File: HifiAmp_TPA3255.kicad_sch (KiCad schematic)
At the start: 123 parts, among them J1 PVDD 48V IN — NEEDS_DATA, J2 RCA L SE, J3 RCA R SE, J301 SPK_L, J302 SPK_R, J4 VOLUME_REMOTE, Q301 IPP330P10NM, Q302 IXTK200N10L2, U1 LM5010ASD, U2 LM2940IMP-12/NOPB, U3 TLV1117-33IDCY, U4 OPA1612AIDR, U5 OPA1612AIDR, U6 TPA3255B, U7 TPS3802K33DCKR, U8 LM5069-2

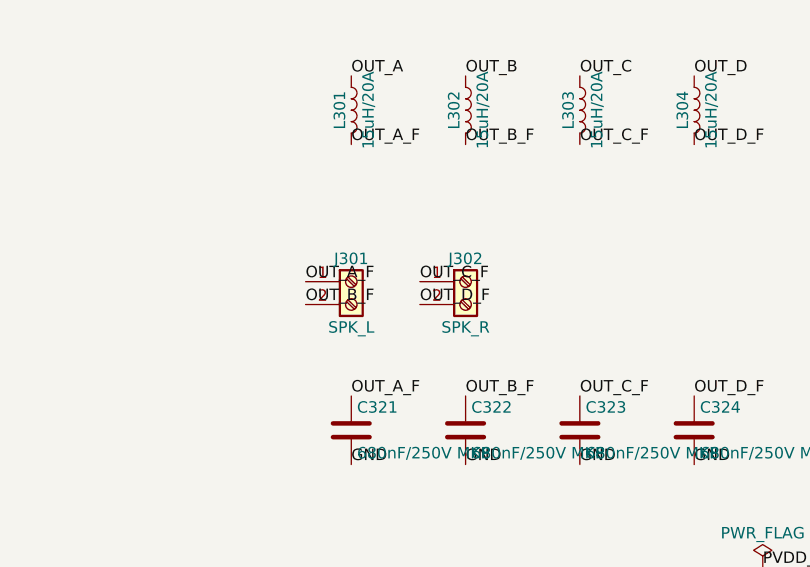
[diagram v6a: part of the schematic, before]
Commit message: feat(e1.11): swap the terminal pins, and find the parity check never ran
The four labels move at J301 and J302 and nowhere else — L301-L304 and C321-C324
keep their nets, which is the check that matters, since swapping there would
have undone the correction. ERC holds at 16 warnings and no error.

The larger finding came from validating it. schematic_parity is an opt-in flag
on kicad-cli pcb drc, and the JSON field reads 0 when the test did not run, so
every "schematic_parity = 0" this project recorded as proof meant "not measured".
The real baseline is 3, all explainable: U6's pin 45 has no pad because the
TPA3255 PowerPAD sits on top of the package, and H1/H2 are mounting holes with
no symbol. Nothing is broken — but a real mismatch would have stayed invisible
just the same. What exposed it was a negative test: change the schematic, skip
the propagation, and watch the report still say 0.

Propagation itself has no automated path. Neither kicad-cli nor the MCP exposes
"Update PCB from Schematic", so the board waits on the user. Board file is
untouched and the schematic edit is committed, so nothing is lost meanwhile.

Co-Authored-By: Claude Opus 5 <noreply@anthropic.com>
Claude-Session: https://claude.ai/code/session_017KEKgkQHHQWX4vViqUxNCh
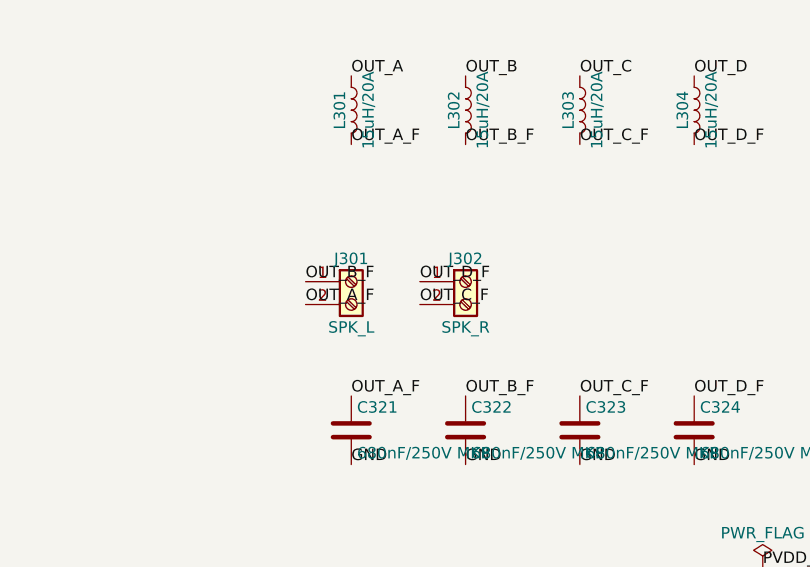
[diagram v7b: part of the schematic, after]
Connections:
- net OUT_A_F: now also J301.2 (Pin_2); no longer J301.1 (Pin_1)
- net OUT_B_F: now also J301.1 (Pin_1); no longer J301.2 (Pin_2)
- net OUT_C_F: now also J302.2 (Pin_2); no longer J302.1 (Pin_1)
- net OUT_D_F: now also J302.1 (Pin_1); no longer J302.2 (Pin_2)
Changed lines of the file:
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@@
 	)
 	(label "OUT_A_F"
-		(at 248.92 364.49 0)
-		(effects
-			(font
-				(size 1.27 1.27)
-			)
-			(justify left bottom)
-		)
-	)
-	(label "OUT_B_F"
-		(at 248.92 367.03 0)
-		(effects
-			(font
-				(size 1.27 1.27)
-			)
-			(justify left bottom)
-		)
-	)
-	(label "OUT_C_F"
-		(at 261.62 364.49 0)
-		(effects
-			(font
-				(size 1.27 1.27)
-			)
-			(justify left bottom)
-		)
-	)
-	(label "OUT_D_F"
-		(at 261.62 367.03 0)
-		(effects
-			(font
-				(size 1.27 1.27)
-			)
-			(justify left bottom)
-		)
-	)
-	(label "OUT_A_F"
 		(at 254 377.19 0)
 		(effects
@@
 		)
 	)
+	(label "OUT_B_F"
+		(at 248.92 364.49 0)
+		(effects
+			(font
+				(size 1.27 1.27)
+			)
+			(justify left bottom)
+		)
+	)
+	(label "OUT_A_F"
+		(at 248.92 367.03 0)
+		(effects
+			(font
+				(size 1.27 1.27)
+			)
+			(justify left bottom)
+		)
+	)
+	(label "OUT_D_F"
+		(at 261.62 364.49 0)
+		(effects
+			(font
+				(size 1.27 1.27)
+			)
+			(justify left bottom)
+		)
+	)
+	(label "OUT_C_F"
+		(at 261.62 367.03 0)
+		(effects
+			(font
+				(size 1.27 1.27)
+			)
+			(justify left bottom)
+		)
+	)
 	(symbol
 		(lib_id "HifiAmp_TPA3255_Local:LM5010ASD")
@@
 			)
 		)
-				(property "MPN" "3403.0285.11"
+		(property "MPN" "3403.0285.11"
 			(at 266.7 320.04 0)
-			(effects (font (size 1.27 1.27)) (hide yes))
+			(effects
+				(font
+					(size 1.27 1.27)
+				)
+				(hide yes)
+			)
 		)
-				(property "Manufacturer" "Schurter"
+		(property "Manufacturer" "Schurter"
 			(at 266.7 320.04 0)
-			(effects (font (size 1.27 1.27)) (hide yes))
+			(effects
+				(font
+					(size 1.27 1.27)
+				)
+				(hide yes)
+			)
 		)
 		(instances
@@
 			)
 		)
-				(property "MPN" "SMDJ58CA"
+		(property "MPN" "SMDJ58CA"
 			(at 279.4 320.04 0)
-			(effects (font (size 1.27 1.27)) (hide yes))
+			(effects
+				(font
+					(size 1.27 1.27)
+				)
+				(hide yes)
+			)
 		)
-				(property "Manufacturer" "Littelfuse"
+		(property "Manufacturer" "Littelfuse"
 			(at 279.4 320.04 0)
-			(effects (font (size 1.27 1.27)) (hide yes))
+			(effects
+				(font
+					(size 1.27 1.27)
+				)
+				(hide yes)
+			)
 		)
 		(instances
@@
 			)
 		)
-				(property "MPN" "IPP330P10NM"
+		(property "MPN" "IPP330P10NM"
 			(at 292.1 320.04 0)
-			(effects (font (size 1.27 1.27)) (hide yes))
+			(effects
+				(font
+					(size 1.27 1.27)
+				)
+				(hide yes)
+			)
 		)
-				(property "Manufacturer" "Infineon"
+		(property "Manufacturer" "Infineon"
 			(at 292.1 320.04 0)
-			(effects (font (size 1.27 1.27)) (hide yes))
+			(effects
+				(font
+					(size 1.27 1.27)
+				)
+				(hide yes)
+			)
 		)
 		(instances
@@
 			)
 		)
-				(property "MPN" "BZT52C15"
+		(property "MPN" "BZT52C15"
 			(at 309.88 325.12 0)
-			(effects (font (size 1.27 1.27)) (hide yes))
+			(effects
+				(font
+					(size 1.27 1.27)
+				)
+				(hide yes)
+			)
 		)
 		(instances
@@
 			)
 		)
-				(property "MPN" "IXTK200N10L2"
+		(property "MPN" "IXTK200N10L2"
 			(at 381 424.18 0)
-			(effects (font (size 1.27 1.27)) (hide yes))
+			(effects
+				(font
+					(size 1.27 1.27)
+				)
+				(hide yes)
+			)
 		)
-				(property "Manufacturer" "Littelfuse/IXYS"
+		(property "Manufacturer" "Littelfuse/IXYS"
 			(at 381 424.18 0)
-			(effects (font (size 1.27 1.27)) (hide yes))
+			(effects
+				(font
+					(size 1.27 1.27)
+				)
+				(hide yes)
+			)
 		)
 		(instances
@@
 			)
 		)
-				(property "MPN" "WSL25124L000FEA"
+		(property "MPN" "WSL25124L000FEA"
 			(at 355.6 403.86 0)
-			(effects (font (size 1.27 1.27)) (hide yes))
+			(effects
+				(font
+					(size 1.27 1.27)
+				)
+				(hide yes)
+			)
 		)
 		(instances
@@
 			)
 		)
-				(property "MPN" "MKS2C044701O00KSSD"
+		(property "MPN" "MKS2C044701O00KSSD"
 			(at 330.2 449.58 0)
-			(effects (font (size 1.27 1.27)) (hide yes))
+			(effects
+				(font
+					(size 1.27 1.27)
+				)
+				(hide yes)
+			)
 		)
 		(instances

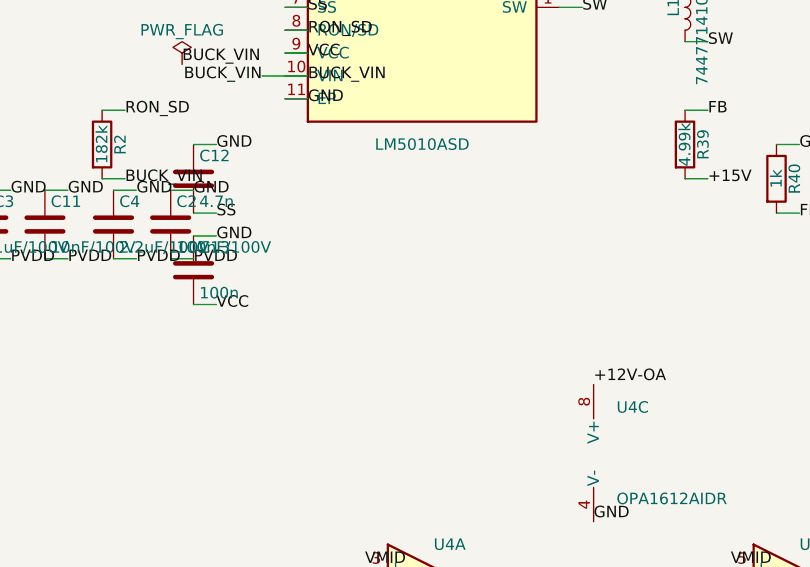
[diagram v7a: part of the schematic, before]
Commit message: feat(f1.6): add the LM5010A input decoupling C327/C328 next to U1
The buck VIN had no local capacitor behind the series Schottky D3. Per
SNVS376F, 0.1 uF + 2.2 uF 100 V now sit at 1.3 mm of U1.10 with ground
straight onto the exposed pad. Parity 3, 78 GND left, ERC unchanged.

Co-Authored-By: Claude Opus 5.5 <noreply@anthropic.com>
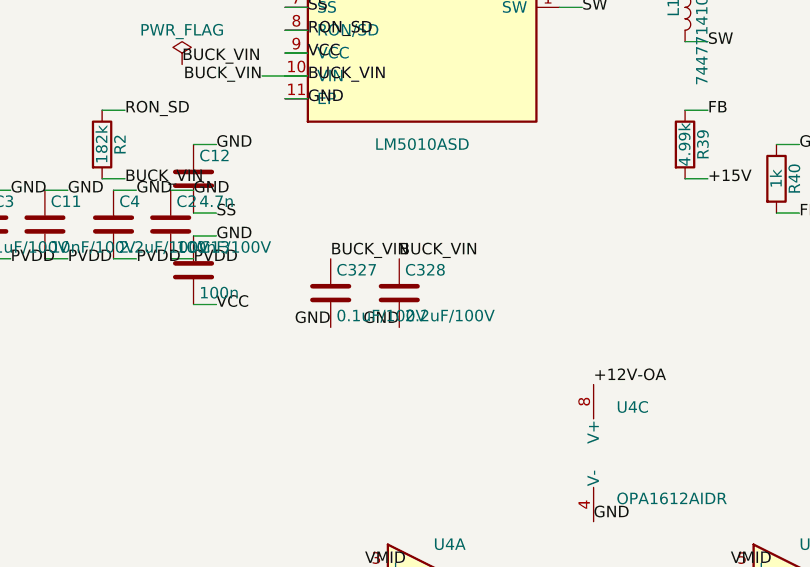
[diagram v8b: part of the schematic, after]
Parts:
- added C327: 0.1uF/100V, Capacitor_SMD:C_0603_1608Metric, symbol Device:C
- added C328: 2.2uF/100V, Capacitor_SMD:C_1210_3225Metric, symbol Device:C
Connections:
- net BUCK_VIN: now also C327.1, C328.1
- net GND: now also C327.2, C328.2
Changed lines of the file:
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@@
 		)
 	)
+	(label "BUCK_VIN"
+		(at 90.17 128.27 0)
+		(effects
+			(font
+				(size 1.27 1.27)
+			)
+			(justify left bottom)
+		)
+	)
+	(label "BUCK_VIN"
+		(at 97.79 128.27 0)
+		(effects
+			(font
+				(size 1.27 1.27)
+			)
+			(justify left bottom)
+		)
+	)
+	(label "GND"
+		(at 90.17 135.89 180)
+		(effects
+			(font
+				(size 1.27 1.27)
+			)
+			(justify right bottom)
+		)
+	)
+	(label "GND"
+		(at 97.79 135.89 180)
+		(effects
+			(font
+				(size 1.27 1.27)
+			)
+			(justify right bottom)
+		)
+	)
 	(symbol
 		(lib_id "HifiAmp_TPA3255_Local:LM5010ASD")
@@
 					(unit 1)
 				)
+			)
+		)
+	)
+	(symbol
+		(lib_id "Device:C")
+		(at 90.17 132.08 0)
+		(unit 1)
+		(in_bom yes)
+		(on_board yes)
+		(dnp no)
+		(property "Reference" "C327"
+			(at 90.805 129.54 0)
+			(effects
+				(font
+					(size 1.27 1.27)
+				)
+				(justify left)
+			)
+		)
+		(property "Value" "0.1uF/100V"
+			(at 90.805 134.62 0)
+			(effects
+				(font
+					(size 1.27 1.27)
+				)
+				(justify left)
+			)
+		)
+		(property "Footprint" "Capacitor_SMD:C_0603_1608Metric"
+			(at 91.1352 135.89 0)
+			(hide yes)
+			(effects
+				(font
+					(size 1.27 1.27)
+				)
+			)
+		)
+		(property "Datasheet" ""
+			(at 90.17 132.08 0)
+			(hide yes)
+			(effects
+				(font
+					(size 1.27 1.27)
+				)
+			)
+		)
+		(instances
+			(project "HifiAmp_TPA3255"
+				(path "/82ac8e0a-ee6a-44b0-87ab-dda432df5a9b"
+					(reference "C327")
+					(unit 1)
+				)
+			)
+		)
+	)
+	(symbol
+		(lib_id "Device:C")
+		(at 97.79 132.08 0)
+		(unit 1)
+		(in_bom yes)
+		(on_board yes)
+		(dnp no)
+		(property "Reference" "C328"
+			(at 98.425 129.54 0)
+			(effects
+				(font
+					(size 1.27 1.27)
+				)
+				(justify left)
+			)
+		)
+		(property "Value" "2.2uF/100V"
+			(at 98.425 134.62 0)
+			(effects
+				(font
+					(size 1.27 1.27)
+				)
+				(justify left)
+			)
+		)
+		(property "Footprint" "Capacitor_SMD:C_1210_3225Metric"
+			(at 98.7552 135.89 0)
+			(hide yes)
+			(effects
+				(font
+					(size 1.27 1.27)
+				)
+			)
+		)
+		(property "Datasheet" ""
+			(at 97.79 132.08 0)
+			(hide yes)
+			(effects
+				(font
+					(size 1.27 1.27)
+				)
+			)
+		)
+		(instances
+			(project "HifiAmp_TPA3255"
+				(path "/82ac8e0a-ee6a-44b0-87ab-dda432df5a9b"
+					(reference "C328")
+					(unit 1)
+				)
